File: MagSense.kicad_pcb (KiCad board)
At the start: 4 copper layers, 36 x 150 mm, 59 parts, among them SW1001 Reset, SW1002 Boot, U0 ESP32-S3-WROOM-1, U1 AP7361C-33ER-13, U2 CD74HC154M96

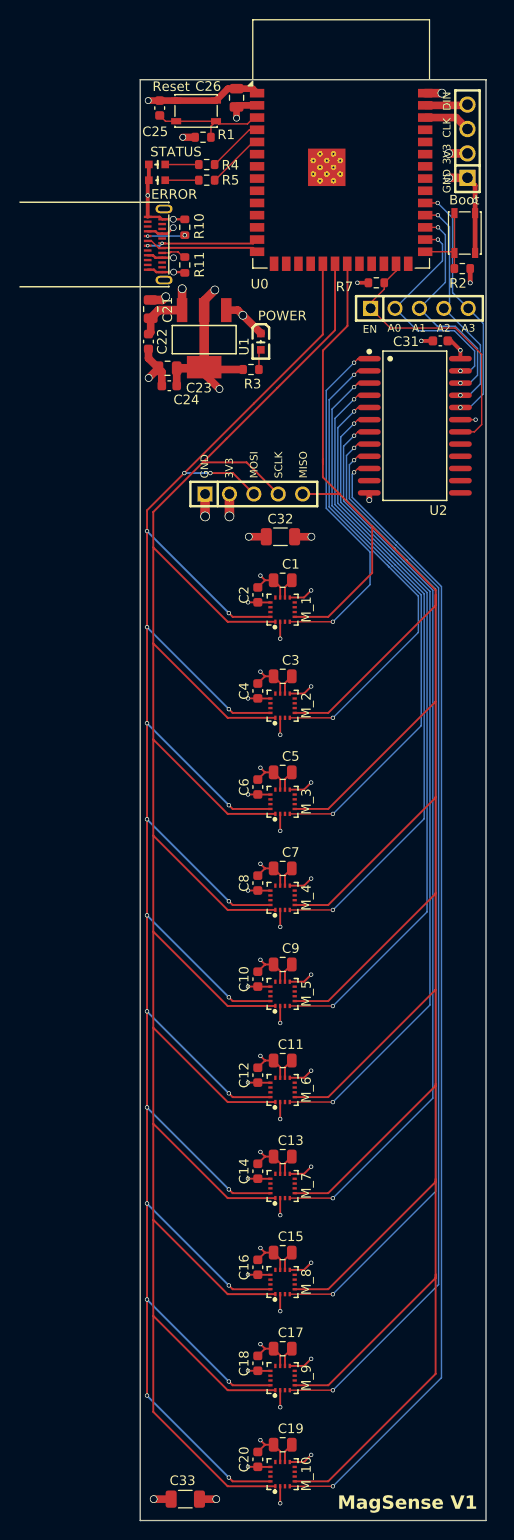
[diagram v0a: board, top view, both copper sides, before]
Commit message: Update PCB layout and footprint changes
Co-Authored-By: Claude Opus 4.6 (1M context) <noreply@anthropic.com>
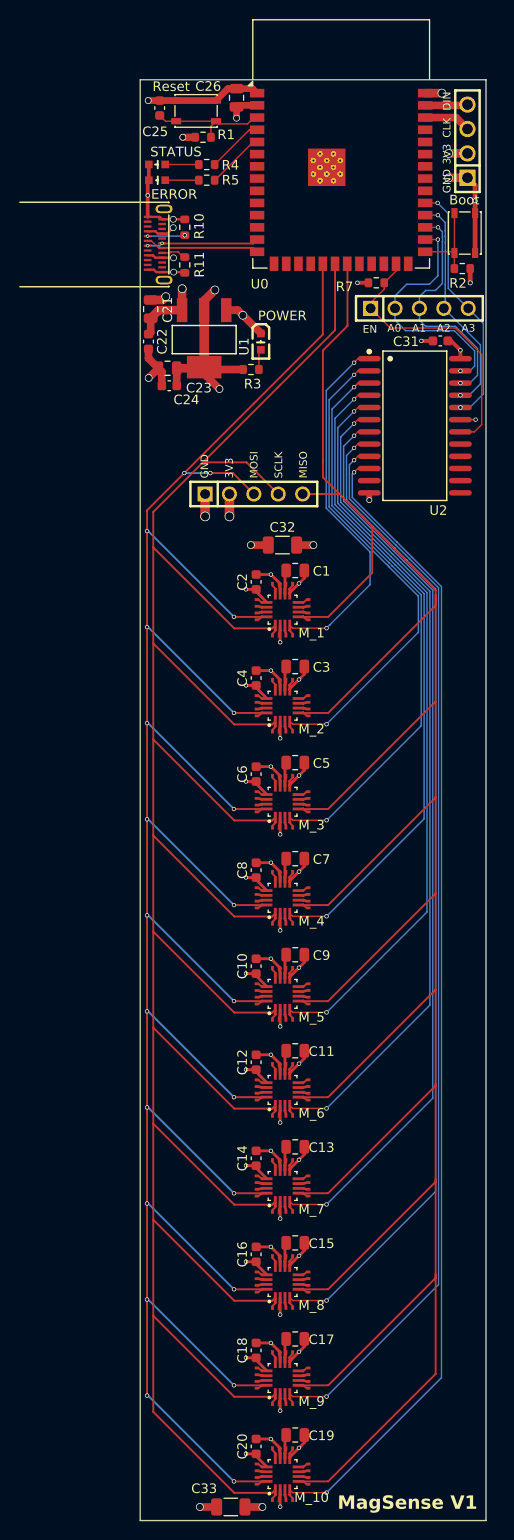
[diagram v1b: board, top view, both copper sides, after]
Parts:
- removed the C19 at (105.6, 211.0)
- removed the C20 at (103.0, 212.5)
- removed the M_10 at (105.6, 214.1)
- added C1: 10uF, Capacitor_SMD:C_0805_2012Metric, F.Cu at (106.9, 120.0)
- added C2: 1uF, Capacitor_SMD:C_0603_1608Metric, F.Cu at (102.8, 121.2)
- added M_1: MMC5983MA, JLCImport:MMC5983MA, F.Cu at (105.6, 124.1)
- moved M_10 90.0 mm to (105.6, 214.1)
- moved C19 89.0 mm to (106.9, 210.0), turned to 0 degrees
- moved C20 88.7 mm to (102.8, 211.2)
- moved C33 4.80 mm to (100.2, 217.5), turned to 180 degrees
- moved C11 1.65 mm to (106.9, 170.0), turned to 0 degrees
- moved C13 1.65 mm to (106.9, 180.0), turned to 0 degrees
- moved C15 1.65 mm to (106.9, 190.0), turned to 0 degrees
- moved C17 1.65 mm to (106.9, 200.0), turned to 0 degrees
- moved C3 1.65 mm to (106.9, 130.0), turned to 0 degrees
- moved C5 1.65 mm to (106.9, 140.0), turned to 0 degrees
- moved C7 1.65 mm to (106.9, 150.0), turned to 0 degrees
- moved C9 1.65 mm to (106.9, 160.0), turned to 0 degrees
- moved C10 1.36 mm to (102.8, 161.2)
- moved C12 1.36 mm to (102.8, 171.2)
- moved C14 1.36 mm to (102.8, 181.2)
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- renumbered C1 to C19, C2 to C20, M_1 to M_10
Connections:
- M_10 pad 4: /10x10 Array/CS_00 -> /10x10 Array/CS_09
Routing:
- net +3V3: track 78.9 -> 84.4 mm
- net /MOSI: track 298.9 -> 294.2 mm
- net /SCLK: track 296.2 -> 300.4 mm
- net /MISO: track 316.7 -> 313.0 mm
- net Net-(M_1-CAP): track 0.00 -> 2.50 mm
- net Net-(M_10-CAP) (its old number): track 2.09 -> 0.00 mm
- net GND: track 131.7 -> 129.8 mm
- net /A0: track 24.1 -> 25.8 mm
- net /A1: track 23.9 -> 25.0 mm
